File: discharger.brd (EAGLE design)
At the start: 35.6 x 69.8 mm, 109 parts, among them U1 BW6101, U10 BW6101, U11 BW6101, U12 BW6101, U2 BW6101, U3 BW6101, U4 BW6101, U5 BW6101, U6 BW6101, U7 BW6101, U8 BW6101, U9 BW6101

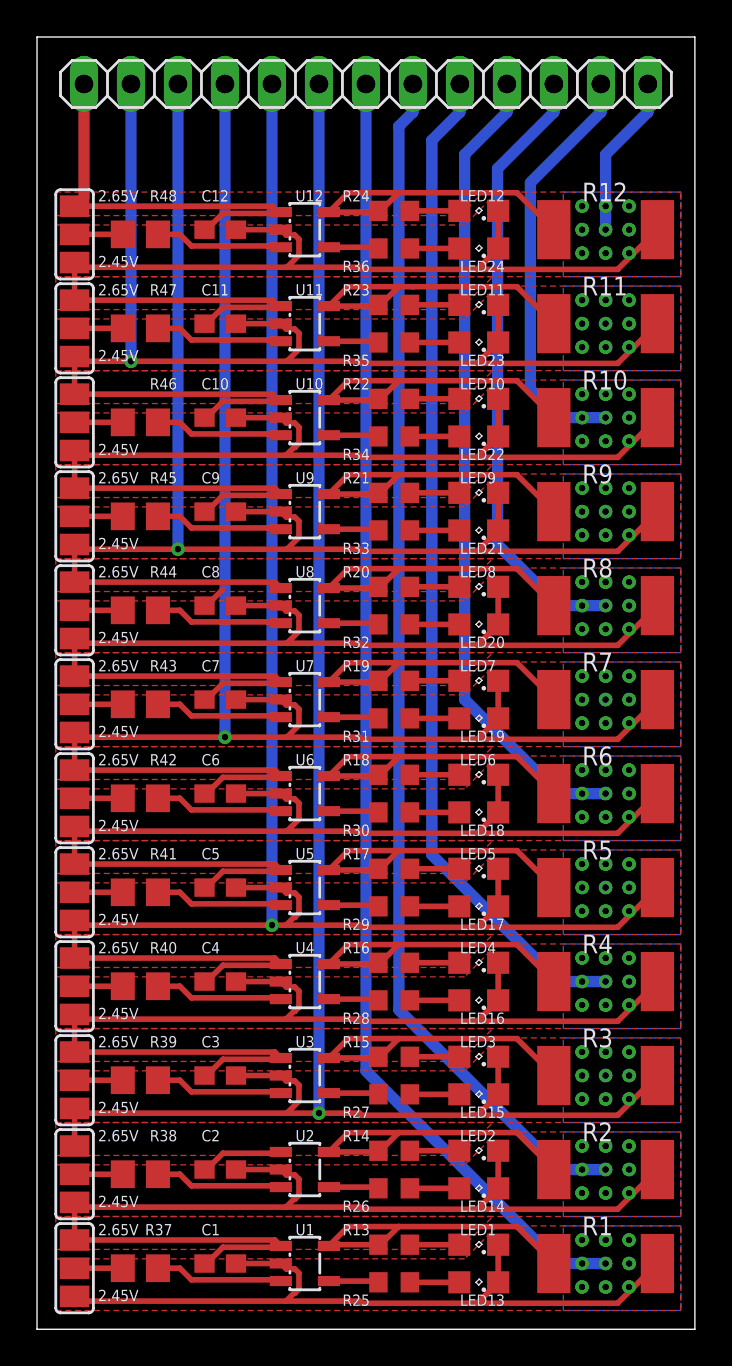
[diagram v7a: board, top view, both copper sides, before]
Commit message: custom parts for LEDs, misc fixes
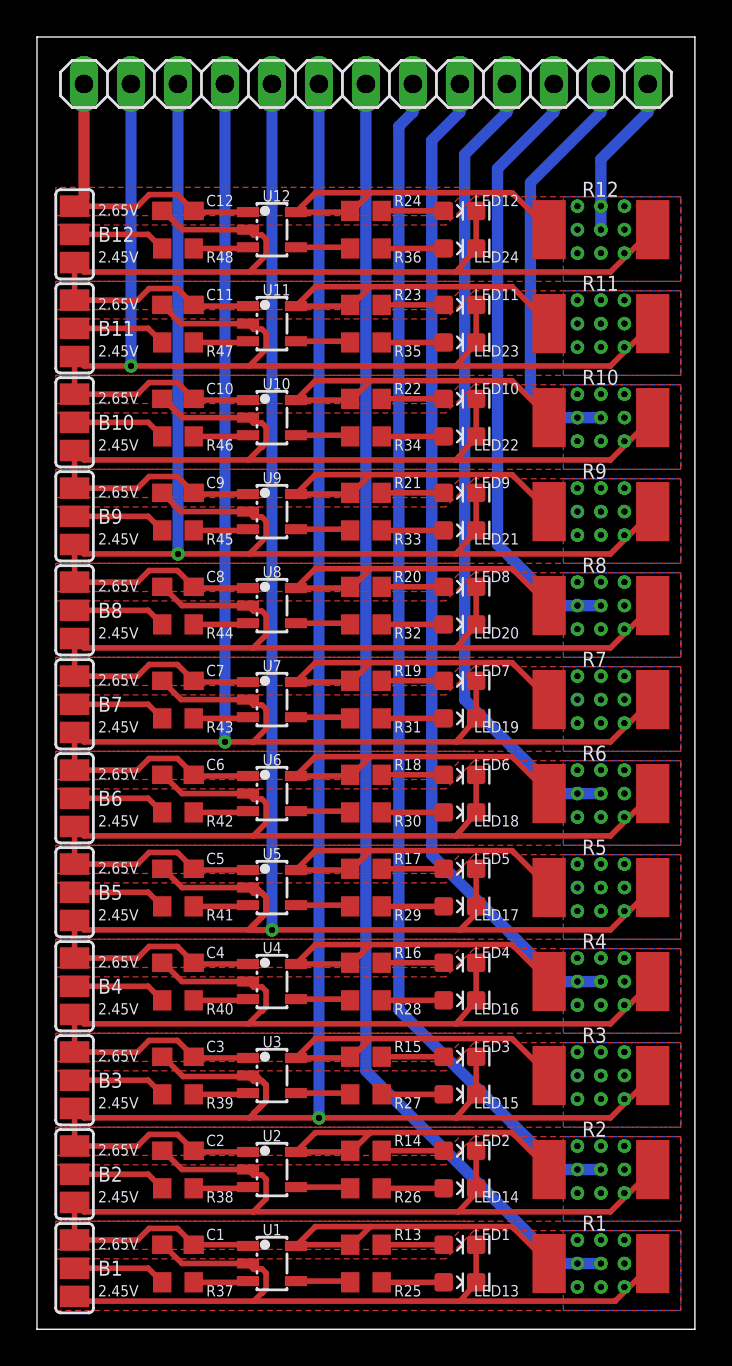
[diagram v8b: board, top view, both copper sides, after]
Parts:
- LED1, LED10, LED11, LED12, LED2, LED3, LED4, LED5, LED6, LED7, LED8, LED9: value BLEED -> Yellow; device led:SML0805 -> ltobms:LED-0603
- LED13, LED14, LED15, LED16, LED17, LED18, LED19, LED20, LED21, LED22, LED23, LED24: value ALARM -> RED; device led:SML0805 -> ltobms:LED-0603
- R13, R14, R15, R16, R17, R18, R19, R20, R21, R22, R23, R24, R25, R26, R27, R28, R29, R30, R31, R32, R33, R34, R35, R36: value 100R -> 100
- R37, R38, R39, R40, R41, R42, R43, R44, R45, R46, R47, R48: value 1K -> 1k; device resistor:R0805 -> resistor:R0603
- moved C9 2.50 mm to (7.62, 45.2), turned to 180 degrees
- moved C4 2.50 mm to (7.62, 19.8), turned to 180 degrees
- moved C6 2.50 mm to (7.62, 30.0), turned to 180 degrees
- moved C1 2.50 mm to (7.62, 4.57), turned to 180 degrees
- moved C2 2.50 mm to (7.62, 9.65), turned to 180 degrees
- moved C3 2.50 mm to (7.62, 14.7), turned to 180 degrees
- moved C10 2.50 mm to (7.62, 50.3), turned to 180 degrees
- moved C11 2.50 mm to (7.62, 55.4), turned to 180 degrees
- moved C12 2.50 mm to (7.62, 60.5), turned to 180 degrees
- moved C5 2.50 mm to (7.62, 24.9), turned to 180 degrees
- moved C7 2.50 mm to (7.62, 35.1), turned to 180 degrees
- moved C8 2.50 mm to (7.62, 40.1), turned to 180 degrees
- moved R39 2.17 mm to (7.62, 12.7)
- moved R40 2.17 mm to (7.62, 17.8)
- moved R41 2.17 mm to (7.62, 22.9)
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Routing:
- net B2: track 103.8 -> 115.4 mm
- net B12: track 22.6 -> 16.8 mm
- net N$53: track 6.93 -> 2.93 mm
- net N$57: track 6.93 -> 2.93 mm
- net N$58: track 6.93 -> 2.93 mm
- net N$55: track 6.93 -> 2.93 mm
- net N$66: track 6.93 -> 2.93 mm
- net N$63: track 6.93 -> 2.93 mm
- net N$62: track 6.93 -> 2.93 mm
- net N$54: track 6.93 -> 2.93 mm
- net N$48: track 6.93 -> 2.93 mm
- net N$47: track 6.93 -> 2.93 mm
- net N$42: track 6.93 -> 2.96 mm
- net N$43: track 6.93 -> 2.96 mm
- net B1: track 124.6 -> 121.3 mm
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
